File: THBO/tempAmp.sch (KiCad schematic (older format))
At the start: 8 parts, among them U201 AD849X

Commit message: Small Misc Changes
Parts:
- R201: value SAT -> 1M
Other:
- moved on the sheet: C201, R201, R203, U201
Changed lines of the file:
@@
 L R R201
 U 1 1 584CBC83
-P 3300 2700
+P 3050 2550
 AR Path="/5866FBDE/584CBC83" Ref="R201"  Part="1"
 AR Path="/58677ED6/584CBC83" Ref="R301"  Part="1"
@@
 AR Path="/586821E6/584CBC83" Ref="R3201"  Part="1"
 AR Path="/586821F4/584CBC83" Ref="R3301"  Part="1"
-F 0 "R201" V 3380 2700 50  0000 C CNN
-F 1 "SAT" V 3300 2700 50  0000 C CNN
-F 2 "Resistors_SMD:R_0603_HandSoldering" V 3230 2700 50  0001 C CNN
-F 3 "" H 3300 2700 50  0000 C CNN
-F 4 "311-1.00MHRCT-ND" V 3300 2700 60  0001 C CNN "Digikey P/N"
-	1    3300 2700
+F 0 "R201" V 3130 2550 50  0000 C CNN
+F 1 "1M" V 3050 2550 50  0000 C CNN
+F 2 "Resistors_SMD:R_0603_HandSoldering" V 2980 2550 50  0001 C CNN
+F 3 "" H 3050 2550 50  0000 C CNN
+F 4 "311-1.00MHRCT-ND" V 3050 2550 60  0001 C CNN "Digikey P/N"
+	1    3050 2550
 	1    0    0    -1
 $EndComp
@@
 L R R203
 U 1 1 584CBCEC
-P 3600 3350
+P 3650 3350
 AR Path="/5866FBDE/584CBCEC" Ref="R203"  Part="1"
 AR Path="/58677ED6/584CBCEC" Ref="R303"  Part="1"
@@
 AR Path="/586821E6/584CBCEC" Ref="R3203"  Part="1"
 AR Path="/586821F4/584CBCEC" Ref="R3303"  Part="1"
-F 0 "R203" V 3680 3350 50  0000 C CNN
-F 1 "150" V 3600 3350 50  0000 C CNN
-F 2 "Resistors_SMD:R_0603_HandSoldering" V 3530 3350 50  0001 C CNN
-F 3 "" H 3600 3350 50  0000 C CNN
-F 4 "311-150HRCT-ND" V 3600 3350 60  0001 C CNN "Digikey P/N"
-	1    3600 3350
+F 0 "R203" V 3730 3350 50  0000 C CNN
+F 1 "150" V 3650 3350 50  0000 C CNN
+F 2 "Resistors_SMD:R_0603_HandSoldering" V 3580 3350 50  0001 C CNN
+F 3 "" H 3650 3350 50  0000 C CNN
+F 4 "311-150HRCT-ND" V 3650 3350 60  0001 C CNN "Digikey P/N"
+	1    3650 3350
 	0    1    1    0
 $EndComp
-Text HLabel 3300 3350 0    60   Input ~ 0
+Text HLabel 2900 3350 0    60   Input ~ 0
 +IN
 $Comp
@@
 L GND #PWR08
 U 1 1 584CBEE6
-P 3550 2550
+P 2750 2450
 AR Path="/5866FBDE/584CBEE6" Ref="#PWR08"  Part="1"
 AR Path="/58677ED6/584CBEE6" Ref="#PWR012"  Part="1"
@@
 AR Path="/586821E6/584CBEE6" Ref="#PWR0128"  Part="1"
 AR Path="/586821F4/584CBEE6" Ref="#PWR0132"  Part="1"
-F 0 "#PWR08" H 3550 2300 50  0001 C CNN
-F 1 "GND" H 3550 2400 50  0000 C CNN
-F 2 "" H 3550 2550 50  0000 C CNN
-F 3 "" H 3550 2550 50  0000 C CNN
-	1    3550 2550
+F 0 "#PWR08" H 2750 2200 50  0001 C CNN
+F 1 "GND" H 2750 2300 50  0000 C CNN
+F 2 "" H 2750 2450 50  0000 C CNN
+F 3 "" H 2750 2450 50  0000 C CNN
+	1    2750 2450
 	1    0    0    -1
 $EndComp
 Text Notes 3850 2450 0    60   ~ 0
 Low Pass Filter\n
-Text HLabel 3300 2900 0    60   Input ~ 0
+Text HLabel 2900 2900 0    60   Input ~ 0
 -IN
 $Comp
 L GND #PWR09
 U 1 1 584CC30B
-P 6350 2800
+P 6250 2750
 AR Path="/5866FBDE/584CC30B" Ref="#PWR09"  Part="1"
 AR Path="/58677ED6/584CC30B" Ref="#PWR013"  Part="1"
@@
 AR Path="/586821E6/584CC30B" Ref="#PWR0129"  Part="1"
 AR Path="/586821F4/584CC30B" Ref="#PWR0133"  Part="1"
-F 0 "#PWR09" H 6350 2550 50  0001 C CNN
-F 1 "GND" H 6350 2650 50  0000 C CNN
-F 2 "" H 6350 2800 50  0000 C CNN
-F 3 "" H 6350 2800 50  0000 C CNN
-	1    6350 2800
-	1    0    0    -1
-$EndComp
-Text GLabel 5400 2200 1    47   Input ~ 0
+F 0 "#PWR09" H 6250 2500 50  0001 C CNN
+F 1 "GND" H 6250 2600 50  0000 C CNN
+F 2 "" H 6250 2750 50  0000 C CNN
+F 3 "" H 6250 2750 50  0000 C CNN
+	1    6250 2750
+	1    0    0    -1
+$EndComp
+Text GLabel 5650 2200 1    47   Input ~ 0
 +5V
 $Comp
 L C C201
 U 1 1 584D00E4
-P 6350 2450
+P 6250 2500
 AR Path="/5866FBDE/584D00E4" Ref="C201"  Part="1"
 AR Path="/58677ED6/584D00E4" Ref="C301"  Part="1"
@@
 AR Path="/586821E6/584D00E4" Ref="C3201"  Part="1"
 AR Path="/586821F4/584D00E4" Ref="C3301"  Part="1"
-F 0 "C201" H 6375 2550 50  0000 L CNN
-F 1 "0.1uF" H 6375 2350 50  0000 L CNN
-F 2 "Capacitors_SMD:C_0603_HandSoldering" H 6388 2300 50  0001 C CNN
-F 3 "" H 6350 2450 50  0000 C CNN
-F 4 "311-1088-1-ND" H 6350 2450 60  0001 C CNN "Digikey P/N"
-	1    6350 2450
+F 0 "C201" H 6275 2600 50  0000 L CNN
+F 1 "0.1uF" H 6275 2400 50  0000 L CNN
+F 2 "Capacitors_SMD:C_0603_HandSoldering" H 6288 2350 50  0001 C CNN
+F 3 "" H 6250 2500 50  0000 C CNN
+F 4 "311-1088-1-ND" H 6250 2500 60  0001 C CNN "Digikey P/N"
+	1    6250 2500
 	-1   0    0    1
 $EndComp
-Text Notes 4900 2300 0    60   ~ 0
+Text Notes 6750 2550 0    60   ~ 0
 0.1uF Caps should be as close to power pins as possible\n
-Text HLabel 5850 3100 2    60   Input ~ 0
+Text HLabel 6100 3100 2    60   Input ~ 0
 OUT
 Wire Wire Line
-	4700 2900 4700 3000
-Wire Wire Line
-	3800 2900 4700 2900
-Wire Wire Line
-	4700 3350 4700 3200
+	4950 2900 4950 3000
+Wire Wire Line
+	3800 2900 4950 2900
+Wire Wire Line
+	4950 3350 4950 3200
 Wire Wire Line
 	4050 3350 4050 3250
@@
 Connection ~ 4050 3350
 Wire Wire Line
-	3750 3350 4700 3350
-Wire Wire Line
-	3450 3350 3300 3350
+	2900 3350 3500 3350
 Wire Wire Line
 	4050 2500 4400 2500
@@
 Connection ~ 4050 2900
 Wire Wire Line
-	3500 2900 3300 2900
-Wire Wire Line
-	3300 2900 3300 2850
-Wire Wire Line
-	3550 2550 3300 2550
+	2900 2900 3500 2900
 Wire Wire Line
 	4400 2500 4400 2650
 Wire Wire Line
-	4700 3100 4600 3100
-Wire Wire Line
-	4600 3100 4600 3600
-Wire Wire Line
-	4600 3600 5850 3600
-Wire Wire Line
-	5850 3600 5850 3100
-Wire Wire Line
-	5400 2200 5400 2650
-Wire Wire Line
-	5300 2650 5300 2500
-Wire Wire Line
-	5300 2500 6100 2500
-Wire Wire Line
-	5400 2300 6350 2300
-Connection ~ 5400 2300
-Wire Wire Line
-	6350 2600 6350 2800
-Wire Wire Line
-	6350 2800 6100 2800
-Connection ~ 6350 2800
-Wire Wire Line
-	6100 2800 6100 2500
-Text Notes 3200 2100 0    60   ~ 0
+	4950 3100 4850 3100
+Wire Wire Line
+	4850 3100 4850 3600
+Wire Wire Line
+	4850 3600 6100 3600
+Wire Wire Line
+	6100 3600 6100 3100
+Wire Wire Line
+	5650 2200 5650 2650
+Wire Wire Line
+	5550 2250 5550 2650
+Connection ~ 5650 2300
+Text Notes 3400 2200 0    60   ~ 0
 Filter Freq, Diff: 505.2 Hz\nFilter Freq, CM: 10610.3 Hz
 $Comp
 L AD849X U201
 U 1 1 584CBAFB
-P 4900 2850
+P 5150 2850
 AR Path="/5866FBDE/584CBAFB" Ref="U201"  Part="1"
 AR Path="/58677ED6/584CBAFB" Ref="U301"  Part="1"
@@
 AR Path="/586821E6/584CBAFB" Ref="U3201"  Part="1"
 AR Path="/586821F4/584CBAFB" Ref="U3301"  Part="1"
-F 0 "U201" H 5650 2900 60  0000 C CNN
-F 1 "AD849X" H 5500 2300 60  0000 C CNN
-F 2 "Housings_SSOP:MSOP-8_3x3mm_Pitch0.65mm" H 4900 2850 60  0001 C CNN
-F 3 "http://www.analog.com/media/en/technical-documentation/data-sheets/AD8494_8495_8496_8497.pdf" H 4900 2850 60  0001 C CNN
-F 4 "AD8497ARMZ-ND" H 4900 2850 60  0001 C CNN "Digikey P/N"
-	1    4900 2850
-	1    0    0    -1
-$EndComp
-Wire Wire Line
-	5200 2650 4900 2650
-Wire Wire Line
-	4900 2650 4900 2550
-Text GLabel 4900 2550 0    60   Input ~ 0
+F 0 "U201" H 5900 2900 60  0000 C CNN
+F 1 "AD849X" H 5750 2300 60  0000 C CNN
+F 2 "Housings_SSOP:MSOP-8_3x3mm_Pitch0.65mm" H 5150 2850 60  0001 C CNN
+F 3 "http://www.analog.com/media/en/technical-documentation/data-sheets/AD8494_8495_8496_8497.pdf" H 5150 2850 60  0001 C CNN
+F 4 "AD8497ARMZ-ND" H 5150 2850 60  0001 C CNN "Digikey P/N"
+	1    5150 2850
+	1    0    0    -1
+$EndComp
+Wire Wire Line
+	5150 2650 5450 2650
+Wire Wire Line
+	5150 2200 5150 2650
+Text GLabel 5150 2200 1    60   Input ~ 0
 Vref
+Wire Wire Line
+	3800 3350 4950 3350
+Wire Wire Line
+	3050 2700 3050 2900
+Connection ~ 3050 2900
+Wire Wire Line
+	2750 2450 2750 2250
+Wire Wire Line
+	2750 2250 3050 2250
+Wire Wire Line
+	3050 2250 3050 2400
+$Comp
+L GND #PWR?
+U 1 1 592B572B
+P 5350 2350
+F 0 "#PWR?" H 5350 2100 50  0001 C CNN
+F 1 "GND" H 5350 2200 50  0000 C CNN
+F 2 "" H 5350 2350 50  0000 C CNN
+F 3 "" H 5350 2350 50  0000 C CNN
+	1    5350 2350
+	1    0    0    -1
+$EndComp
+Wire Wire Line
+	5550 2250 5350 2250
+Wire Wire Line
+	5350 2250 5350 2350
+Wire Wire Line
+	6250 2750 6250 2650
+Wire Wire Line
+	6250 2350 6250 2300
+Wire Wire Line
+	6250 2300 5650 2300
 $EndSCHEMATC

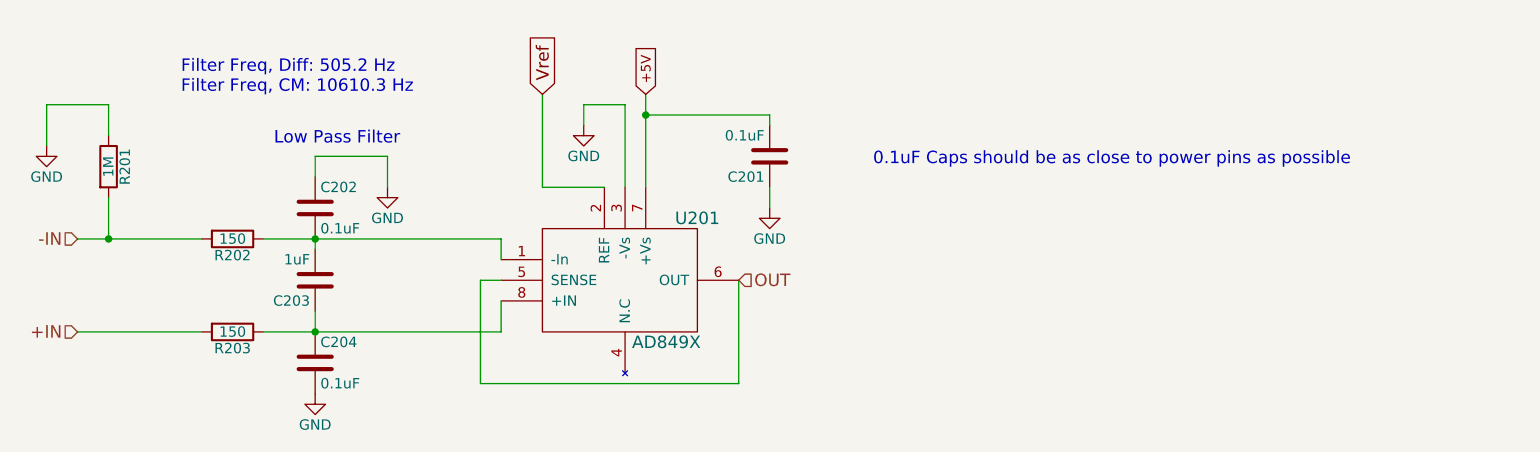
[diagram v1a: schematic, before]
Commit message: Updated THBO to Rev2
-Split the board into two parts to allow for better placement on the
pod.
-Added LEDs to 5V line
-Added pin headers at the input terminals to easily put the board into
self-reference mode using jumpers
-Changed Vref from 0.64V to 1.25V
-Updated schematic to modular design
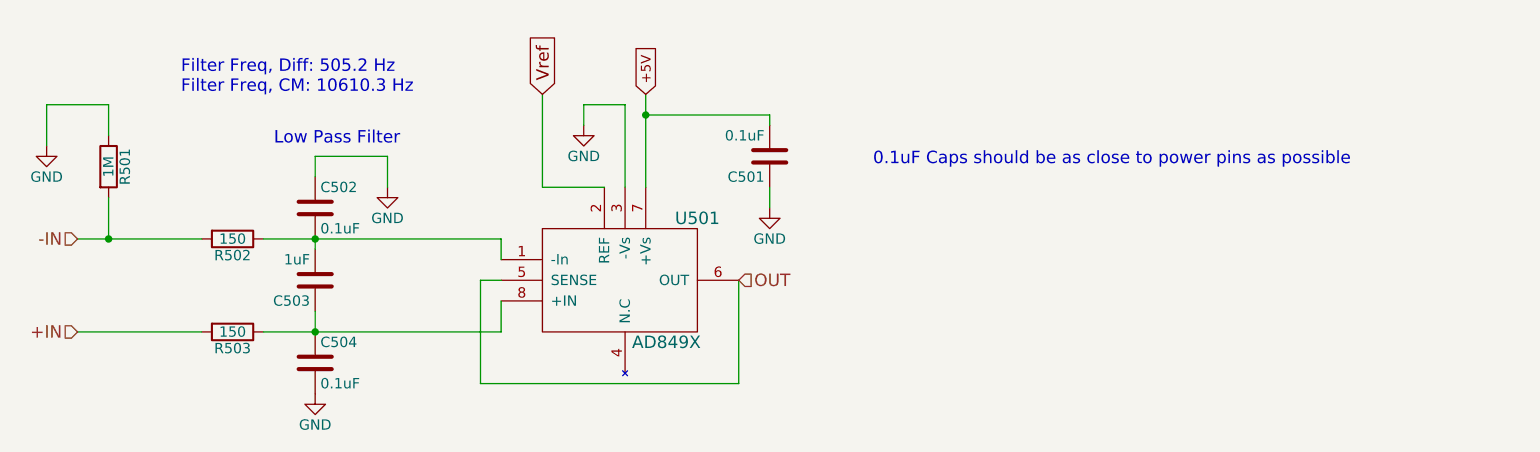
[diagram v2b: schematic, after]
